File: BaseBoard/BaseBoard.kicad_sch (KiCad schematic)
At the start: 54 parts, among them J1 USB_C_DEALON-USB-US31-106, J2 Serial Port, J3 base connector, Q1 PMN48XP, Q2 SSM6L820R, SW1 Battery switch, SW2 boot, SW3 Reset, U1 ESP32-WROOM-E, U3 MCP73831-2ACI-OT, U4 XC6210B332MR

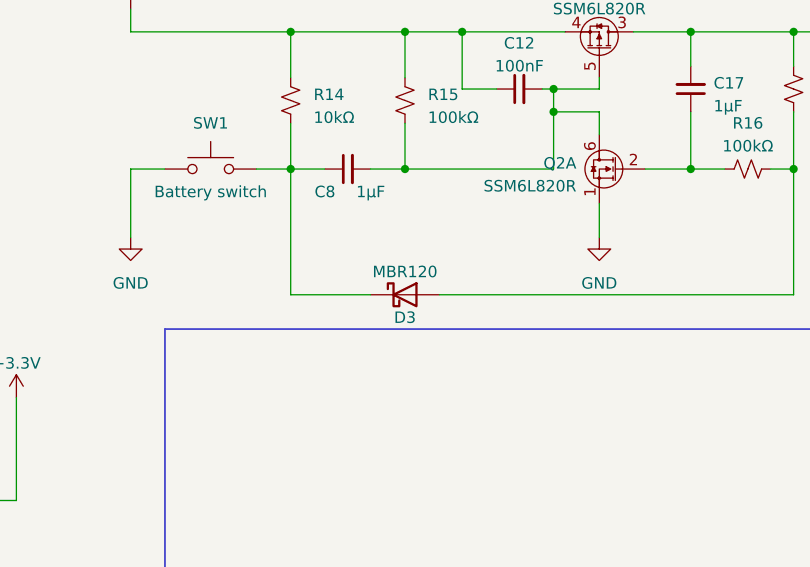
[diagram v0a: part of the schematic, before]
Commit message: Replaces MBR120 in power latch circuit for a BAS20
This is much cheaper and should be enough for this part of the circuit.
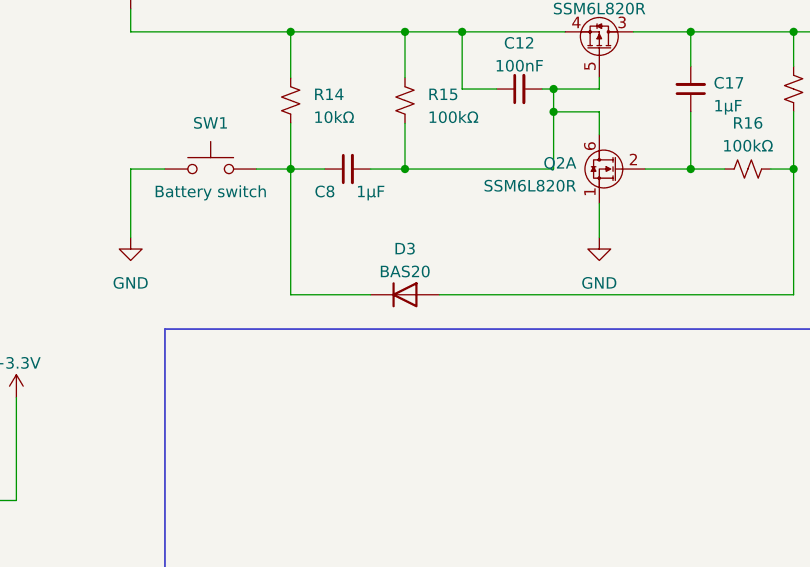
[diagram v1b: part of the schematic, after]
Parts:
- removed D3: MBR120, Diode_SMD:D_SOD-123, symbol Device:D_Schottky
- added D3: BAS20, Package_TO_SOT_SMD:SOT-23, symbol Diode:BAS20
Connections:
- net at C8.1, R14.2, SW1.2: now also D3.3 (K)
- net at R16.2, R17.1: now also D3.1 (A)

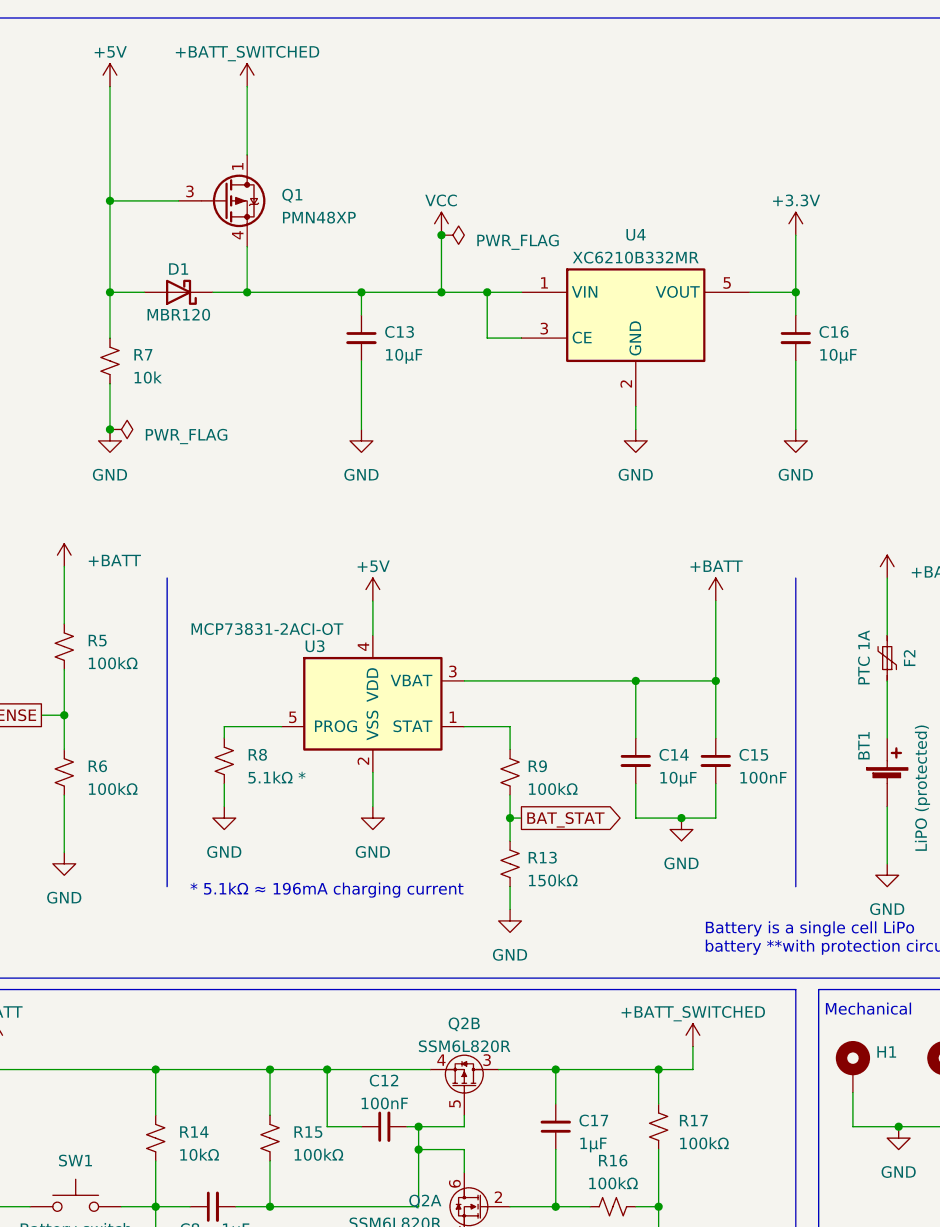
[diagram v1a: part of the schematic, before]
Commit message: Renames new power symbol to battery_switched
This also fixes the pin assignement inside the symbol.
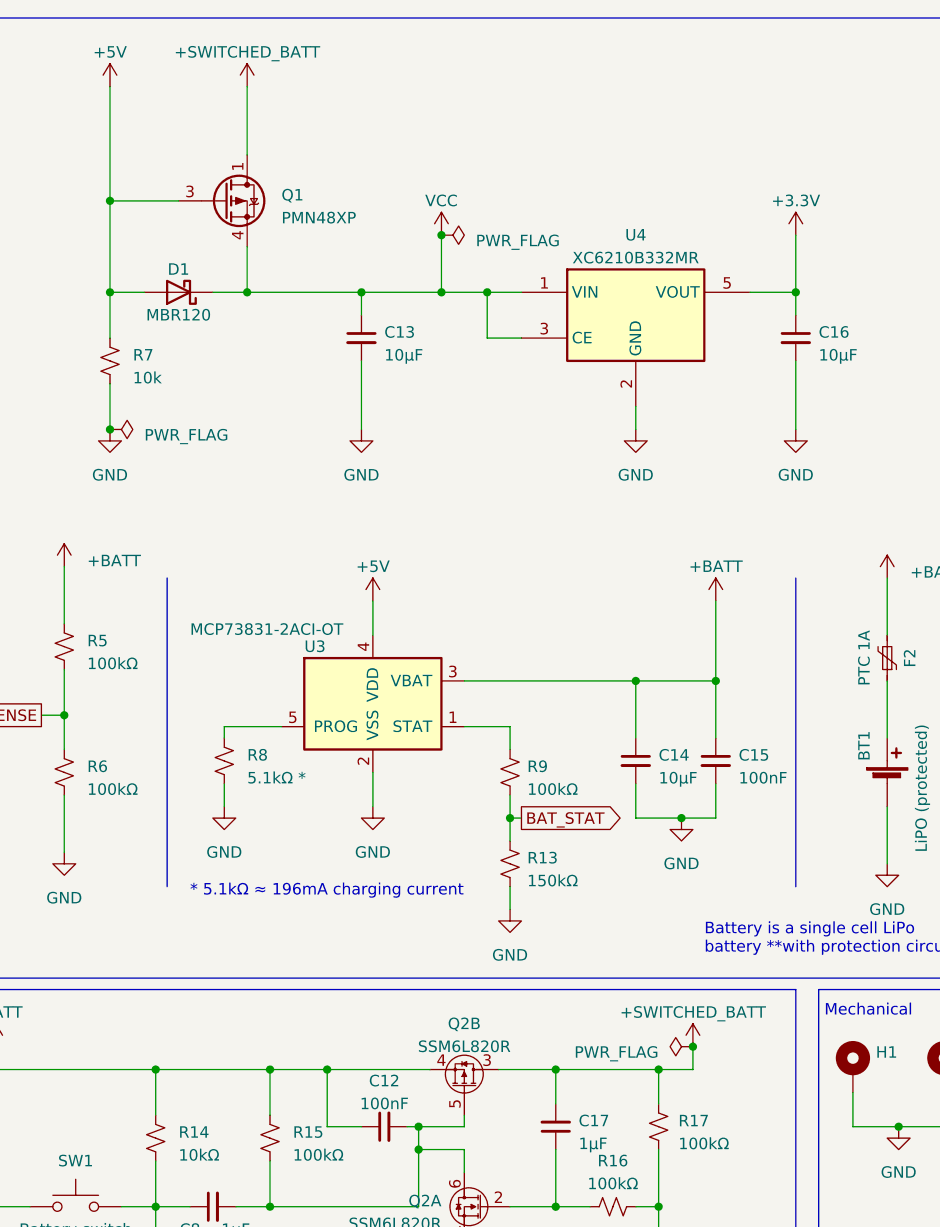
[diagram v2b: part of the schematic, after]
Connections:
- net +BATT: no longer C17.2, Q1.1 (D), Q1.2 (D), Q1.5 (D), Q1.6 (D), Q2.3 (D), R17.2
- new net +SWITCHED_BATT: C17.2, Q1.1 (D), Q1.2 (D), Q1.5 (D), Q1.6 (D), Q2.3 (D), R17.2

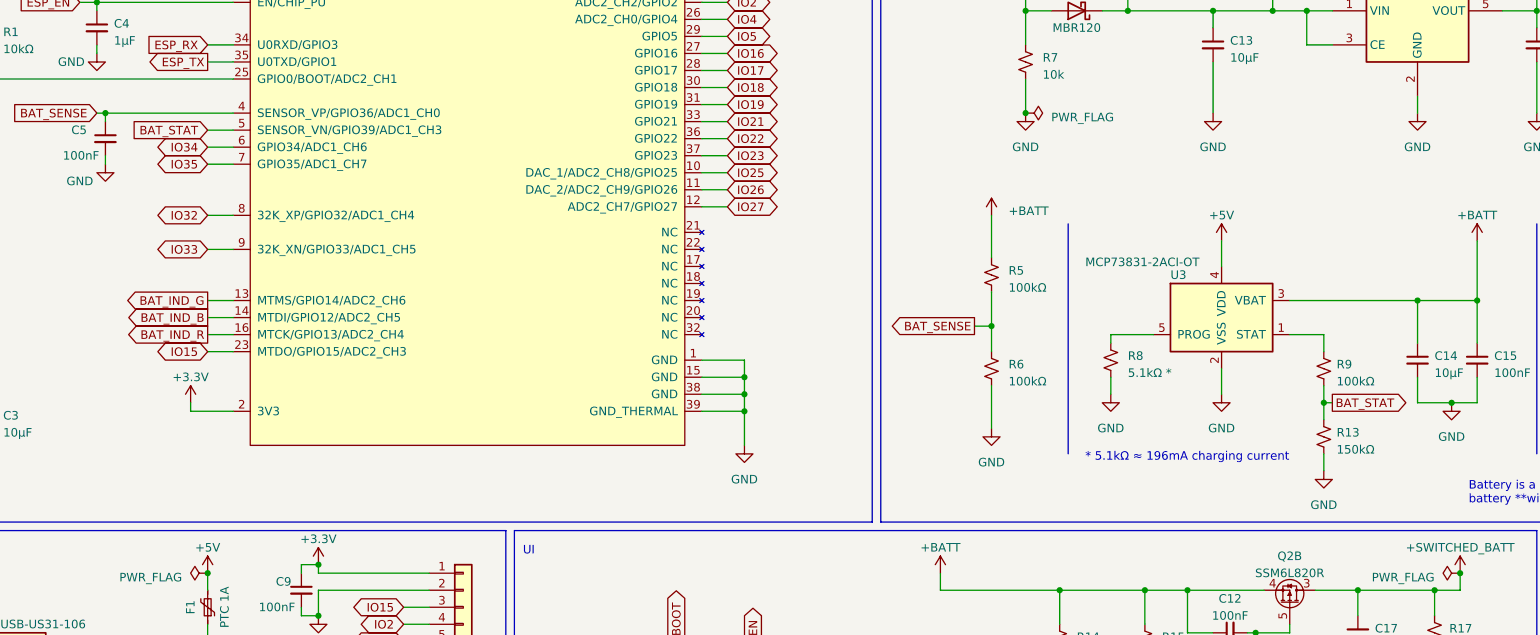
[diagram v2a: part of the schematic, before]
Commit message: Uses fixed LED to indicate charging status instead of the uC
We're now using a single led to indicate if the battery is currently
being charged. It will turn off as soon as the battery is fully charged.
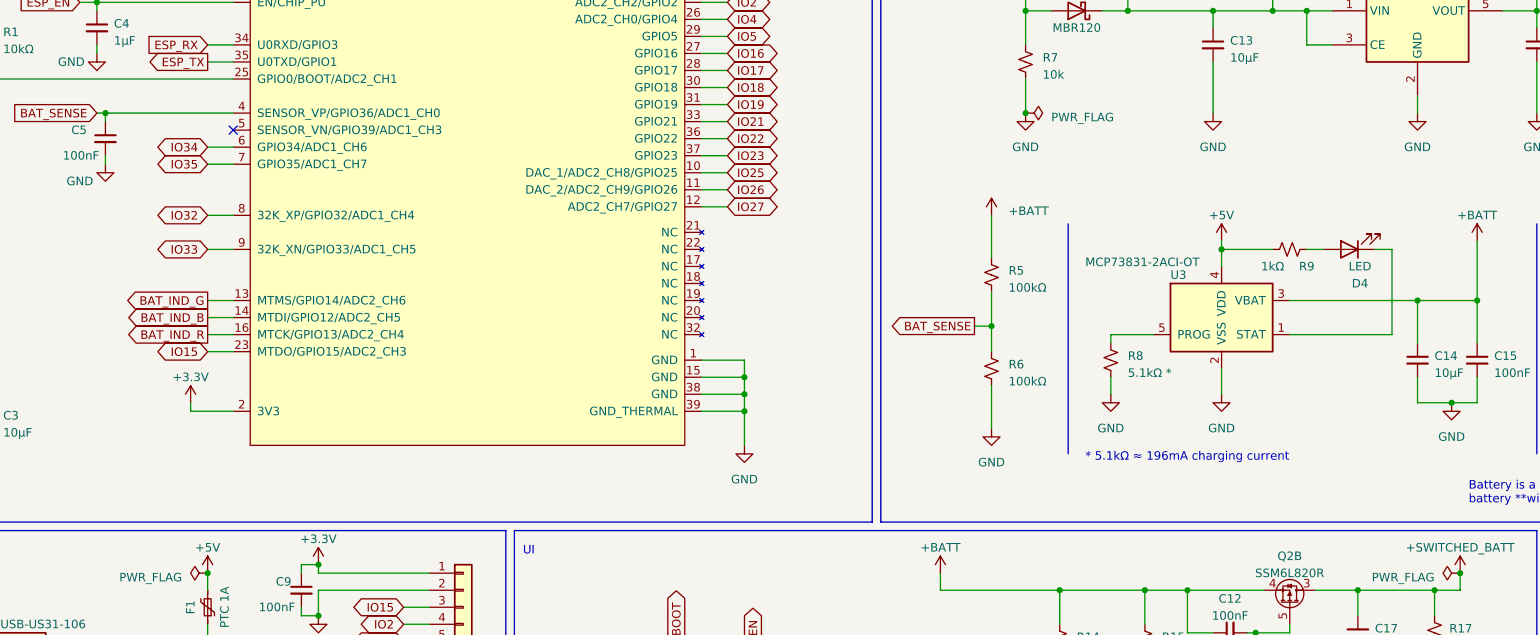
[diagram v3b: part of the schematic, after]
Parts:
- removed R13: 150kΩ, Resistor_SMD:R_0805_2012Metric_Pad1.20x1.40mm_HandSolder, symbol Device:R_Small_US
- added D4: LED, LED_SMD:LED_0603_1608Metric, symbol Device:LED
- R9: value 100kΩ -> 1kΩ
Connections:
- net +5V: now also R9.2
- net at U3.1 (STAT): now also D4.1 (K); no longer R9.1
- net BAT_STAT: no longer names the net of U1.5 (SENSOR_VN/GPIO39/ADC1_CH3)
- net BAT_STAT: no longer R9.2
- new net: D4.2 (A), R9.1
- no-connect marks 0 -> 1

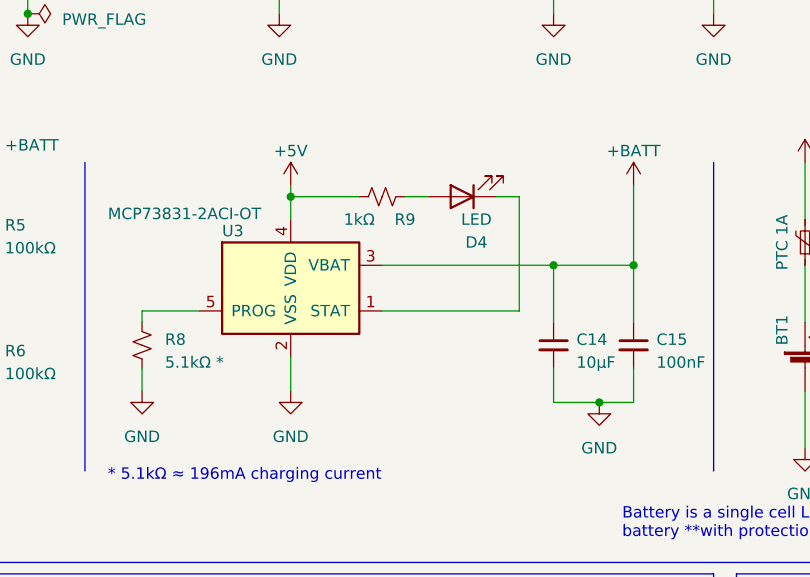
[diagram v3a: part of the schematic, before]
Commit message: Adds green battery status LED
This LED will light up when battery is done charging.
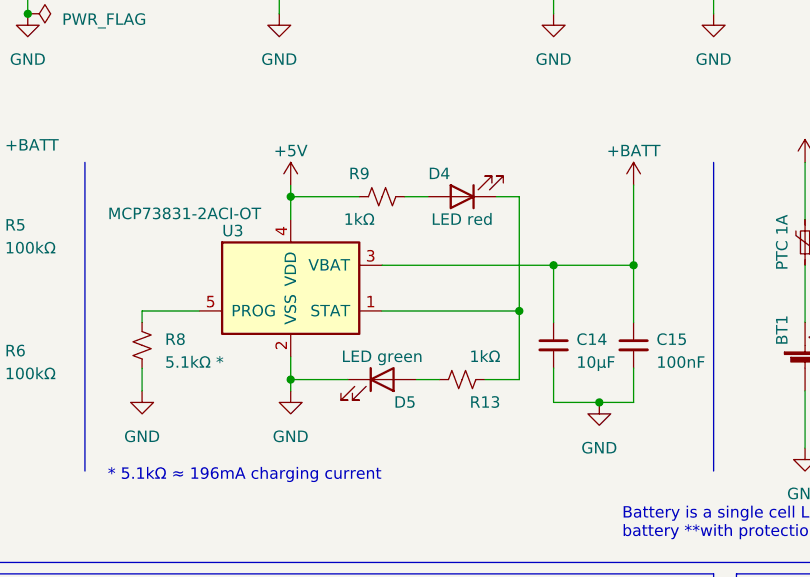
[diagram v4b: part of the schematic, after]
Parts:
- added D5: LED green, LED_SMD:LED_0603_1608Metric, symbol Device:LED
- added R13: 1kΩ, Resistor_SMD:R_0805_2012Metric_Pad1.20x1.40mm_HandSolder, symbol Device:R_Small_US
- D4: value LED -> LED red
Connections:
- net GND: now also D5.1 (K)
- net at D4.1 (K), U3.1 (STAT): now also R13.2
- new net: D5.2 (A), R13.1

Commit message: Updates all schematic PDFs to version 1.0
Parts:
- ?: renamed from C10; value 100nF -> (none); footprint Capacitor_SMD:C_0805_2012Metric_Pad1.18x1.45mm_HandSolder -> (none)
- ?: renamed from D4; value LED red -> (none); footprint LED_SMD:LED_0603_1608Metric -> (none)
- ?: renamed from R12; value 1kΩ -> (none); footprint Resistor_SMD:R_0805_2012Metric_Pad1.20x1.40mm_HandSolder -> (none)
- ?: renamed from SW3; value Reset -> (none); footprint GameOver:SW_Tactile_SPST_SOFNG_TS-1814 -> (none)
- ?: renamed from R8; value 5.1kΩ * -> (none); footprint Resistor_SMD:R_0805_2012Metric_Pad1.20x1.40mm_HandSolder -> (none)
- ?: renamed from SW1; value Battery switch -> (none); footprint GameOver:SW_Tactile_SPST_SOFNG_TS-1814 -> (none)
- ?: renamed from R2; value 10kΩ -> (none); footprint Resistor_SMD:R_0805_2012Metric_Pad1.20x1.40mm_HandSolder -> (none)
- ?: renamed from C7; value 4.7µF -> (none); footprint Capacitor_SMD:C_0805_2012Metric_Pad1.18x1.45mm_HandSolder -> (none)
- ?: renamed from C16; value 10µF -> (none); footprint Capacitor_SMD:C_0805_2012Metric_Pad1.18x1.45mm_HandSolder -> (none)
- ?: renamed from F2; value PTC 1A -> (none); footprint GameOver:Belfuse_0ZCJ -> (none)
- ?: renamed from C4; value 1µF -> (none); footprint Capacitor_SMD:C_0805_2012Metric_Pad1.18x1.45mm_HandSolder -> (none)
- ?: renamed from H2; value ~ -> (none); footprint MountingHole:MountingHole_2.2mm_M2_Pad_Via -> (none)
- ? (x2): renamed from Q2; value SSM6L820R -> (none); footprint GameOver:TSOP6F -> (none)
- ?: renamed from C13; value 10µF -> (none); footprint Capacitor_SMD:C_0805_2012Metric_Pad1.18x1.45mm_HandSolder -> (none)
- ?: renamed from C11; value 100nF -> (none); footprint Capacitor_SMD:C_0805_2012Metric_Pad1.18x1.45mm_HandSolder -> (none)
- ?: renamed from R14; value 10kΩ -> (none); footprint Resistor_SMD:R_0805_2012Metric_Pad1.20x1.40mm_HandSolder -> (none)
- ?: renamed from R4; value 5.1kΩ -> (none); footprint Resistor_SMD:R_0805_2012Metric_Pad1.20x1.40mm_HandSolder -> (none)
- ?: renamed from D2; value LED_BGAR -> (none); footprint GameOver:Hongzhi_Forest_HS-1204-RGB -> (none)
- ?: renamed from R6; value 100kΩ -> (none); footprint Resistor_SMD:R_0805_2012Metric_Pad1.20x1.40mm_HandSolder -> (none)
- ?: renamed from C5; value 100nF -> (none); footprint Capacitor_SMD:C_0805_2012Metric_Pad1.18x1.45mm_HandSolder -> (none)
- ?: renamed from R13; value 1kΩ -> (none); footprint Resistor_SMD:R_0805_2012Metric_Pad1.20x1.40mm_HandSolder -> (none)
- ?: renamed from C14; value 10µF -> (none); footprint Capacitor_SMD:C_0805_2012Metric_Pad1.18x1.45mm_HandSolder -> (none)
- ?: renamed from C1; value 100nF -> (none); footprint Capacitor_SMD:C_0805_2012Metric_Pad1.18x1.45mm_HandSolder -> (none)
- ?: renamed from R10; value 1kΩ -> (none); footprint Resistor_SMD:R_0805_2012Metric_Pad1.20x1.40mm_HandSolder -> (none)
- ?: renamed from H1; value ~ -> (none); footprint MountingHole:MountingHole_2.2mm_M2_Pad_Via -> (none)
- ?: renamed from C3; value 10µF -> (none); footprint Capacitor_SMD:C_0805_2012Metric_Pad1.18x1.45mm_HandSolder -> (none)
- ?: renamed from Q1; value PMN48XP -> (none); footprint Package_SO:TSOP-6_1.65x3.05mm_P0.95mm -> (none)
- ?: renamed from R11; value 1kΩ -> (none); footprint Resistor_SMD:R_0805_2012Metric_Pad1.20x1.40mm_HandSolder -> (none)
- ?: renamed from D3; value BAS20 -> (none); footprint Package_TO_SOT_SMD:SOT-23 -> (none)
- ?: renamed from U1; value ESP32-WROOM-E -> (none); footprint Espressif:ESP32-WROOM-32E -> (none)
- ?: renamed from C8; value 1µF -> (none); footprint Capacitor_SMD:C_0805_2012Metric_Pad1.18x1.45mm_HandSolder -> (none)
- ?: renamed from R9; value 1kΩ -> (none); footprint Resistor_SMD:R_0805_2012Metric_Pad1.20x1.40mm_HandSolder -> (none)
- ?: renamed from R15; value 100kΩ -> (none); footprint Resistor_SMD:R_0805_2012Metric_Pad1.20x1.40mm_HandSolder -> (none)
- ?: renamed from C17; value 1µF -> (none); footprint Capacitor_SMD:C_0805_2012Metric_Pad1.18x1.45mm_HandSolder -> (none)
- ?: renamed from J2; value Serial Port -> (none); footprint Connector:Tag-Connect_TC2030-IDC-FP_2x03_P1.27mm_Vertical -> (none)
- ?: renamed from C15; value 100nF -> (none); footprint Capacitor_SMD:C_0805_2012Metric_Pad1.18x1.45mm_HandSolder -> (none)
- ?: renamed from C6; value 100nF -> (none); footprint Capacitor_SMD:C_0805_2012Metric_Pad1.18x1.45mm_HandSolder -> (none)
- ?: renamed from C2; value 100nF -> (none); footprint Capacitor_SMD:C_0805_2012Metric_Pad1.18x1.45mm_HandSolder -> (none)
- ?: renamed from J3; value base connector -> (none); footprint GameOver:Base_conn_TXGA_FFC05036-24SBD113W5M_1x24_P0.50mm_Horizontal -> (none)
- ?: renamed from BT1; value LiPO (protected) -> (none); footprint Connector_JST:JST_PH_S2B-PH-SM4-TB_1x02-1MP_P2.00mm_Horizontal -> (none)
- ?: renamed from U4; value XC6210B332MR -> (none); footprint Package_TO_SOT_SMD:SOT-23-5 -> (none)
- ?: renamed from D1; value MBR120 -> (none); footprint Diode_SMD:D_SOD-123 -> (none)
- ?: renamed from J1; value USB_C_DEALON-USB-US31-106 -> (none); footprint GameOver:DEALON_USB-US31-106 -> (none)
- ?: renamed from F1; value PTC 1A -> (none); footprint GameOver:Belfuse_0ZCJ -> (none)
- ?: renamed from LOGO1; value GameOver_logo -> (none); footprint GameOver:logo_fsilk -> (none)
- ?: renamed from R5; value 100kΩ -> (none); footprint Resistor_SMD:R_0805_2012Metric_Pad1.20x1.40mm_HandSolder -> (none)
- ?: renamed from C12; value 100nF -> (none); footprint Capacitor_SMD:C_0805_2012Metric_Pad1.18x1.45mm_HandSolder -> (none)
- ?: renamed from U3; value MCP73831-2ACI-OT -> (none); footprint Package_TO_SOT_SMD:SOT-23-5 -> (none)
- ?: renamed from R1; value 10kΩ -> (none); footprint Resistor_SMD:R_0805_2012Metric_Pad1.20x1.40mm_HandSolder -> (none)
- ?: renamed from C9; value 100nF -> (none); footprint Capacitor_SMD:C_0805_2012Metric_Pad1.18x1.45mm_HandSolder -> (none)
- ?: renamed from R17; value 100kΩ -> (none); footprint Resistor_SMD:R_0805_2012Metric_Pad1.20x1.40mm_HandSolder -> (none)
- ?: renamed from D5; value LED green -> (none); footprint LED_SMD:LED_0603_1608Metric -> (none)
- ?: renamed from R16; value 100kΩ -> (none); footprint Resistor_SMD:R_0805_2012Metric_Pad1.20x1.40mm_HandSolder -> (none)
- ?: renamed from SW2; value boot -> (none); footprint GameOver:SW_Tactile_SPST_SOFNG_TS-1814 -> (none)
- ?: renamed from R7; value 10k -> (none); footprint Resistor_SMD:R_0805_2012Metric_Pad1.20x1.40mm_HandSolder -> (none)
- ?: renamed from R3; value 5.1kΩ -> (none); footprint Resistor_SMD:R_0805_2012Metric_Pad1.20x1.40mm_HandSolder -> (none)
